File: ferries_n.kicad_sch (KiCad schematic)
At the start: 48 parts

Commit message: PCBA prototype order
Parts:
- LED401: value Bremerton -> WS2812B-Mini; Ferry Port (none) -> Bremerton
- LED415: value Seattle (Bremerton) -> WS2812B-Mini; Ferry Port (none) -> Seattle (Bremerton)
- LED416: value Westlake Center -> WS2812B-2020; Monorail (none) -> Westlake Center
- LED420: value Seattle Center -> WS2812B-2020; Monorail (none) -> Seattle Center
- LED421: value Seattle (Bainbridge) -> WS2812B-Mini; Ferry Port (none) -> Seattle (Bainbridge)
- LED433: value Bainbridge -> WS2812B-Mini; Ferry Port (none) -> Bainbridge
- LED434: value Kingston -> WS2812B-Mini; Ferry Port (none) -> Kingston
- LED447: value Edmonds -> WS2812B-Mini; Ferry Port (none) -> Edmonds
- renumbered C18 to C401, C19 to C402
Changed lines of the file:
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@@
 		(on_board yes)
 		(dnp no)
-		(fields_autoplaced yes)
 		(property "Reference" "LED420"
 			(at 130.81 69.85 0)
@@
 			)
 		)
-		(property "Value" "Seattle Center"
+		(property "Value" "WS2812B-2020"
 			(at 130.81 72.39 0)
 			(effects
@@
 					(size 1.27 1.27)
 				)
+				(hide yes)
 			)
 		)
@@
 			)
 		)
+		(property "Monorail" "Seattle Center"
+			(at 132.08 72.39 0)
+			(effects
+				(font
+					(size 1.27 1.27)
+				)
+			)
+		)
 		(pin "1"
 		)
@@
 		(on_board yes)
 		(dnp no)
-		(property "Reference" "C19"
+		(property "Reference" "C402"
 			(at 19.05 171.45 90)
 			(effects
@@
 			(project "transit"
 				(path "/3763eade-a8c8-4ec0-9cf2-9db4442b4ee5/91ae385e-b417-4a19-b535-f6364aa8f223"
-					(reference "C19")
+					(reference "C402")
 					(unit 1)
 				)
@@
 			)
 		)
-		(property "Value" "Seattle (Bremerton)"
+		(property "Value" "WS2812B-Mini"
 			(at 30.48 72.39 0)
 			(effects
@@
 					(size 1.27 1.27)
 				)
+				(hide yes)
 			)
 		)
@@
 			)
 		)
+		(property "Ferry Port" "Seattle (Bremerton)"
+			(at 30.48 72.39 0)
+			(effects
+				(font
+					(size 1.27 1.27)
+				)
+			)
+		)
 		(pin "3"
 		)
@@
 			)
 		)
-		(property "Value" "Bremerton"
+		(property "Value" "WS2812B-Mini"
 			(at 49.53 24.13 0)
 			(effects
@@
 					(size 1.27 1.27)
 				)
+				(hide yes)
 			)
 		)
@@
 			)
 		)
+		(property "Ferry Port" "Bremerton"
+			(at 49.53 24.13 0)
+			(effects
+				(font
+					(size 1.27 1.27)
+				)
+			)
+		)
 		(pin "3"
 		)
@@
 		(on_board yes)
 		(dnp no)
-		(property "Reference" "C18"
+		(property "Reference" "C401"
 			(at 17.78 29.21 90)
 			(effects
@@
 			(project "transit"
 				(path "/3763eade-a8c8-4ec0-9cf2-9db4442b4ee5/91ae385e-b417-4a19-b535-f6364aa8f223"
-					(reference "C18")
+					(reference "C401")
 					(unit 1)
 				)
@@
 			)
 		)
-		(property "Value" "Seattle (Bainbridge)"
+		(property "Value" "WS2812B-Mini"
 			(at 29.21 95.25 0)
 			(effects
@@
 			)
 		)
+		(property "Ferry Port" "Seattle (Bainbridge)"
+			(at 39.37 97.79 0)
+			(effects
+				(font
+					(size 1.27 1.27)
+				)
+				(hide yes)
+			)
+		)
 		(pin "3"
 		)
@@
 			)
 		)
-		(property "Value" "Kingston"
+		(property "Value" "WS2812B-Mini"
 			(at 52.07 116.84 0)
 			(effects
@@
 					(size 1.27 1.27)
 				)
+				(hide yes)
 			)
 		)
@@
 			)
 		)
+		(property "Ferry Port" "Kingston"
+			(at 52.07 116.84 0)
+			(effects
+				(font
+					(size 1.27 1.27)
+				)
+			)
+		)
 		(pin "3"
 		)
@@
 		(on_board yes)
 		(dnp no)
-		(fields_autoplaced yes)
 		(property "Reference" "LED416"
 			(at 52.07 69.85 0)
@@
 			)
 		)
-		(property "Value" "Westlake Center"
+		(property "Value" "WS2812B-2020"
 			(at 52.07 72.39 0)
 			(effects
@@
 					(size 1.27 1.27)
 				)
+				(hide yes)
 			)
 		)
@@
 			)
 		)
+		(property "Monorail" "Westlake Center"
+			(at 54.61 72.39 0)
+			(effects
+				(font
+					(size 1.27 1.27)
+				)
+			)
+		)
 		(pin "1"
 		)
@@
 			)
 		)
-		(property "Value" "Bainbridge"
+		(property "Value" "WS2812B-Mini"
 			(at 27.94 116.84 0)
 			(effects
@@
 			)
 		)
+		(property "Ferry Port" "Bainbridge"
+			(at 38.1 119.38 0)
+			(effects
+				(font
+					(size 1.27 1.27)
+				)
+				(hide yes)
+			)
+		)
 		(pin "3"
 		)
@@
 			)
 		)
-		(property "Value" "Edmonds"
+		(property "Value" "WS2812B-Mini"
 			(at 35.56 163.83 0)
 			(effects
@@
 					(size 1.27 1.27)
 				)
+				(hide yes)
 			)
 		)
@@
 			)
 		)
+		(property "Ferry Port" "Edmonds"
+			(at 35.56 163.83 0)
+			(effects
+				(font
+					(size 1.27 1.27)
+				)
+			)
+		)

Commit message: Sounder and T silk, before scripting
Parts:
- removed LED419: WS2812B-2020, EasyEDA:LED-SMD_4P-L2.0-W2.0-TL_WS2812B-2020, symbol EasyEDA:WS2812B-2020
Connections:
- net at LED420.3 (DI): now also LED418.1 (DO)
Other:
- moved on the sheet: LED420

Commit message: sounder layout checkpoint
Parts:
- removed C401, C402: 150u, EasyEDA:CAP-SMD_L3.5-W2.8, symbol EasyEDA:CL21B106KOQNNNE
- removed LED401, LED415, LED421, LED433, LED434, LED447: WS2812B-Mini, EasyEDA:LED-SMD_4P-L3.5-W3.5-TL_WS2812B, symbol EasyEDA:WS2812B-MINI
- removed LED402, LED403, LED404, LED405, LED406, LED407, LED408, LED409, LED410, LED411, LED412, LED413, LED414, LED422, LED423, LED424, LED425, LED426, LED427, LED428, LED429, LED431, LED432, LED435, LED436, LED437, LED438, LED439, LED440, LED441, LED442, LED443, LED444, LED445, LED446: WS2812B-2020, EasyEDA:LED-SMD_4P-L2.0-W2.0-TL_WS2812B-2020, symbol EasyEDA:WS2812B-2020
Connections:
- no-connect marks 1 -> 0

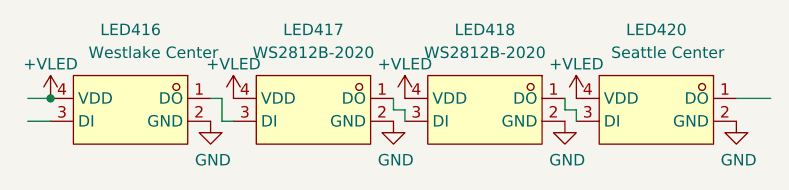
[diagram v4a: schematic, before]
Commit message: Add rail labels
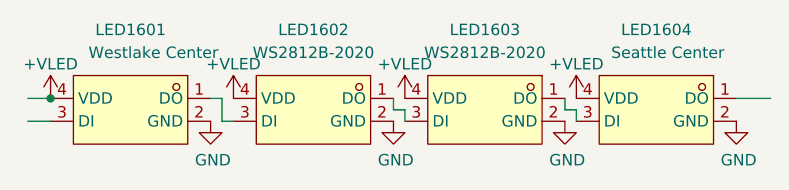
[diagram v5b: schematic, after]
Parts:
- renumbered LED416 to LED1601, LED417 to LED1602, LED418 to LED1603, LED420 to LED1604
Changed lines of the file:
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@@
 		(dnp no)
 		(fields_autoplaced yes)
-		(property "Reference" "LED417"
+		(property "Reference" "LED1602"
 			(at 72.39 69.85 0)
 			(show_name no)
@@
 			(project "transit"
 				(path "/3763eade-a8c8-4ec0-9cf2-9db4442b4ee5/153adc6e-a3b0-4527-a19a-87e28aab4b4d/91ae385e-b417-4a19-b535-f6364aa8f223"
-					(reference "LED417")
+					(reference "LED1602")
 					(unit 1)
 				)
@@
 		(in_pos_files yes)
 		(dnp no)
-		(property "Reference" "LED420"
+		(property "Reference" "LED1604"
 			(at 110.49 69.85 0)
 			(show_name no)
@@
 			(project "transit"
 				(path "/3763eade-a8c8-4ec0-9cf2-9db4442b4ee5/153adc6e-a3b0-4527-a19a-87e28aab4b4d/91ae385e-b417-4a19-b535-f6364aa8f223"
-					(reference "LED420")
+					(reference "LED1604")
 					(unit 1)
 				)
@@
 		(in_pos_files yes)
 		(dnp no)
-		(property "Reference" "LED416"
+		(property "Reference" "LED1601"
 			(at 52.07 69.85 0)
 			(show_name no)
@@
 			(project "transit"
 				(path "/3763eade-a8c8-4ec0-9cf2-9db4442b4ee5/153adc6e-a3b0-4527-a19a-87e28aab4b4d/91ae385e-b417-4a19-b535-f6364aa8f223"
-					(reference "LED416")
+					(reference "LED1601")
 					(unit 1)
 				)
@@
 		(dnp no)
 		(fields_autoplaced yes)
-		(property "Reference" "LED418"
+		(property "Reference" "LED1603"
 			(at 91.44 69.85 0)
 			(show_name no)
@@
 			(project "transit"
 				(path "/3763eade-a8c8-4ec0-9cf2-9db4442b4ee5/153adc6e-a3b0-4527-a19a-87e28aab4b4d/91ae385e-b417-4a19-b535-f6364aa8f223"
-					(reference "LED418")
-					(unit 1)
-				)
+					(reference "LED1603")
+					(unit 1)
+				)

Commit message: route T
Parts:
- renumbered LED1601 to LED2001, LED1602 to LED2002, LED1603 to LED2003, LED1604 to LED2004
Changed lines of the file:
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@@
 		(dnp no)
 		(fields_autoplaced yes)
-		(property "Reference" "LED1602"
+		(property "Reference" "LED2002"
 			(at 72.39 69.85 0)
 			(show_name no)
@@
 			(project "transit"
 				(path "/3763eade-a8c8-4ec0-9cf2-9db4442b4ee5/153adc6e-a3b0-4527-a19a-87e28aab4b4d/91ae385e-b417-4a19-b535-f6364aa8f223"
-					(reference "LED1602")
+					(reference "LED2002")
 					(unit 1)
 				)
@@
 		(in_pos_files yes)
 		(dnp no)
-		(property "Reference" "LED1604"
+		(property "Reference" "LED2004"
 			(at 110.49 69.85 0)
 			(show_name no)
@@
 			(project "transit"
 				(path "/3763eade-a8c8-4ec0-9cf2-9db4442b4ee5/153adc6e-a3b0-4527-a19a-87e28aab4b4d/91ae385e-b417-4a19-b535-f6364aa8f223"
-					(reference "LED1604")
+					(reference "LED2004")
 					(unit 1)
 				)
@@
 		(in_pos_files yes)
 		(dnp no)
-		(property "Reference" "LED1601"
+		(property "Reference" "LED2001"
 			(at 52.07 69.85 0)
 			(show_name no)
@@
 			(project "transit"
 				(path "/3763eade-a8c8-4ec0-9cf2-9db4442b4ee5/153adc6e-a3b0-4527-a19a-87e28aab4b4d/91ae385e-b417-4a19-b535-f6364aa8f223"
-					(reference "LED1601")
+					(reference "LED2001")
 					(unit 1)
 				)
@@
 		(dnp no)
 		(fields_autoplaced yes)
-		(property "Reference" "LED1603"
+		(property "Reference" "LED2003"
 			(at 91.44 69.85 0)
 			(show_name no)
@@
 			(project "transit"
 				(path "/3763eade-a8c8-4ec0-9cf2-9db4442b4ee5/153adc6e-a3b0-4527-a19a-87e28aab4b4d/91ae385e-b417-4a19-b535-f6364aa8f223"
-					(reference "LED1603")
-					(unit 1)
-				)
+					(reference "LED2003")
+					(unit 1)
+				)

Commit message: route monorail
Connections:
- net SOUNDER_N_MONORAIL: now reaches LED2004.1 (DO)
- net MONORAIL_SOUNDER_N: now reaches LED2001.3 (DI)
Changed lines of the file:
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@@
 	(generator_version "10.0")
 	(paper "A4")
-	(junction
-		(at 43.18 77.47)
-		(diameter 0)
-		(color 0 0 0 0)
-	)
 	(wire
 		(pts
@@
 	(wire
 		(pts
-			(xy 40.64 77.47) (xy 43.18 77.47)
-		)
-		(stroke
-			(width 0)
-			(type default)
-		)
-	)
-	(wire
-		(pts
-			(xy 119.38 77.47) (xy 123.19 77.47)
+			(xy 119.38 77.47) (xy 120.65 77.47)
 		)
 		(stroke
@@
 		)
 	)
+	(global_label "MONORAIL_SOUNDER_N"
+		(shape input)
+		(at 40.64 80.01 180)
+		(fields_autoplaced yes)
+		(effects
+			(font
+				(size 1.27 1.27)
+			)
+			(justify right)
+		)
+		(property "Intersheetrefs" "${INTERSHEET_REFS}"
+			(at 16.0647 80.01 0)
+			(hide yes)
+			(show_name no)
+			(do_not_autoplace no)
+			(effects
+				(font
+					(size 1.27 1.27)
+				)
+				(justify right)
+			)
+		)
+	)
+	(global_label "SOUNDER_N_MONORAIL"
+		(shape input)
+		(at 120.65 77.47 0)
+		(fields_autoplaced yes)
+		(effects
+			(font
+				(size 1.27 1.27)
+			)
+			(justify left)
+		)
+		(property "Intersheetrefs" "${INTERSHEET_REFS}"
+			(at 145.2253 77.47 0)
+			(hide yes)
+			(show_name no)
+			(do_not_autoplace no)
+			(effects
+				(font
+					(size 1.27 1.27)
+				)
+				(justify left)
+			)
+		)
+	)

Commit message: rev-b validation run
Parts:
- LED2001: LCSC Part C965555 -> C52917434; Monorail Westlake Center -> Seattle Center
- LED2002, LED2003: LCSC Part C965555 -> C52917434
- LED2004: LCSC Part C965555 -> C52917434; Monorail Seattle Center -> Westlake Center
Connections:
- net MONORAIL_SOUNDER_N: now also LED2004.1 (DO); no longer LED2001.3 (DI)
- net SOUNDER_N_MONORAIL: now also LED2001.3 (DI); no longer LED2004.1 (DO)
